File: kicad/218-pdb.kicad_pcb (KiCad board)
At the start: 2 copper layers, 97.8 x 72.4 mm, 80 parts, among them J1 Conn_01x03, J10 Conn_01x03, J11 Conn_01x03, J12 Conn_01x03, J13 Conn_01x03, J14 Conn_01x03, J15 Conn_01x03, J16 Conn_01x03, J17 Conn_01x03, J18 Conn_01x03, J19 Conn_01x03, J2 Conn_01x03, J20 Conn_01x03, J21 Conn_01x03, J22 Conn_01x03, J23 Conn_01x03, J24 Conn_01x03, J25 Conn_01x04_Pin, J26 Conn_01x04_Pin, J27 external 5V, J28 14v, J29 14v, J3 Conn_01x03, J30 14v, J31 14v, J32 battery, J33 battery, J4 Conn_01x03, J5 Conn_01x03, J6 Conn_01x03, J7 Conn_01x03, J8 Conn_01x03, J9 Conn_01x03, SW1 5V switch, U1 DC-DC buck, U2 DC-DC buck, U3 TLV76133DCY, U4 TLV76133DCY, U5 TLV76150DCY, U6 TLV76150DCY

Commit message: add fuse terminal
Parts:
- added Fuse1: fuse, 218-pdb:CUI_TB007-508-02BE, F.Cu at (151.5, 114.3)
- FID1, FID2, FID3, FID4: value one 90 degree header pin -> 90 degree header pin
- moved R2 14.1 mm to (78.6, 112.3)
- moved main1 10.4 mm to (140.7, 114.3)
- moved J31 7.50 mm to (129.7, 115.3)
- moved J30 6.78 mm to (118.9, 115.3)
- moved J29 6.11 mm to (108.2, 115.3)
- moved J28 5.36 mm to (97.5, 115.3)
- moved NT2 5.07 mm to (147.9, 102.9), turned to -90 degrees
- moved R5 4.90 mm to (92.4, 112.5)
- moved D6 4.68 mm to (90.6, 119.9)
- moved D5 1.89 mm to (84.5, 119.9)
- moved J26 0.13 mm to (78.6, 75.6)
- moved J25 0.13 mm to (78.6, 106.0)
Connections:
- J32 pad 1: +BATT -> Net-(Fuse1-Pin_2)
- NT2 pad 1: 14-3 -> 14-1
- NT2 pad 3: 14-1 -> 14-3
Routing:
- net Net-(J32-Pin_2): track 6.35 -> 0.00 mm
- net 5-3: track 81.2 -> 75.4 mm
- net 14-3: track 27.0 -> 25.5 mm
- net Net-(D6-K): track 7.15 -> 5.63 mm
- net Net-(D5-K): track 8.97 -> 7.94 mm
- net +BATT: track 32.3 -> 31.3 mm
- net 14-1: track 102.1 -> 102.9 mm
- net 5-2: track 86.5 -> 87.1 mm
- added copper zone on F.Cu, net Net-(Fuse1-Pin_2)
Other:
- board text added: "FUSE"
- board text added: "MAIN SWITCH"
- board text removed: "switch and fuse"

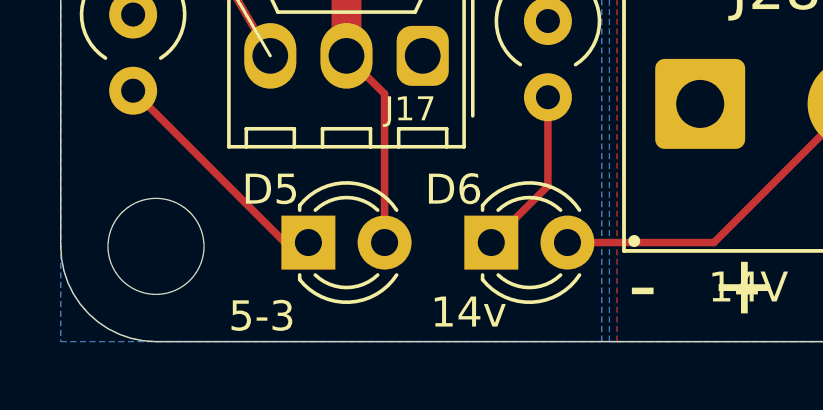
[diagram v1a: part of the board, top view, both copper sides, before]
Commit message: align silkscreen and comment schematic
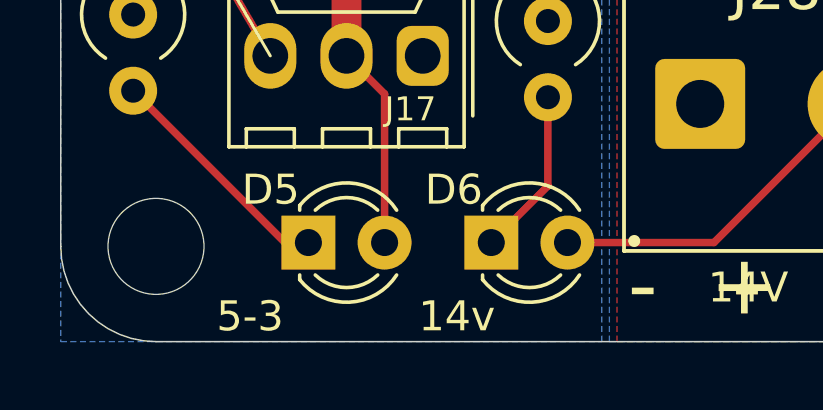
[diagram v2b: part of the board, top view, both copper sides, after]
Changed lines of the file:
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@@
 	)
 	(gr_text "5-3"
-		(at 81.788 122.936 0)
+		(at 81.389683 122.934687 0)
 		(layer "F.SilkS")
 		(effects
@@
 	)
 	(gr_text "14v"
-		(at 88.519 122.809 0)
+		(at 88.12488 122.934687 0)
 		(layer "F.SilkS")
 		(effects

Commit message: change jst xh model
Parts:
- J1, J10, J11, J12, J13, J14, J15, J16, J2, J3, J4, J5, J6, J7, J8, J9: footprint 218-pdb:JST_XH_B3B-XH-A_1x03_P2.50mm_Vertical -> 218-pdb:JST_XH_B3B-XH-AM_1x03_P2.50mm_Vertical
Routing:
- net 5-1: track 92.8 -> 94.3 mm
- net 5-2: track 87.1 -> 88.4 mm

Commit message: advice from Karl
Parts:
- C9: value 10 uF -> 220 uF; footprint Capacitor_THT:C_Disc_D3.8mm_W2.6mm_P2.50mm -> Capacitor_THT:CP_Radial_D5.0mm_P2.50mm
- moved C9 28.3 mm to (85.1, 54.0), turned to 0 degrees
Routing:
- net 5-3: track 75.4 -> 82.1 mm
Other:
- board text added: "5V"
- board text added: "G"
- board text added: "S"
- board text removed: "S 5V G"
